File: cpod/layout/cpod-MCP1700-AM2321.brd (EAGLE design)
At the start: 11 parts

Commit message: 换用独石电容
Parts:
- moved R1 5.08 mm to (38.1, -29.2)
- moved AM2321 5.08 mm to (39.4, -31.8)
- moved MCP1700T 5.08 mm to (34.3, -34.3)
- moved C1 2.54 mm to (33.0, -36.8)
- moved C2 2.54 mm to (38.1, -36.8)
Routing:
- net GND: track 89.5 -> 84.4 mm
- net VCC: track 58.9 -> 53.8 mm
- net SDA: track 15.2 -> 20.3 mm
- net RAW: track 14.8 -> 10.8 mm
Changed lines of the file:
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@@
 </autorouter>
 <elements>
-<element name="AM2321" library="SparkFun-Connectors" package="1X04" value="" x="39.37" y="-26.67" rot="R180"/>
-<element name="MCP1700T" library="SparkFun-Connectors" package="1X03" value="+3V3" x="34.29" y="-29.21"/>
+<element name="AM2321" library="SparkFun-Connectors" package="1X04" value="" x="39.37" y="-31.75" rot="R180"/>
+<element name="MCP1700T" library="SparkFun-Connectors" package="1X03" value="+3V3" x="34.29" y="-34.29"/>
 <element name="ARDUINO1" library="SparkFun-Connectors" package="1X12" value="M12PTH" x="31.75" y="-16.51"/>
 <element name="ARDUINO2" library="SparkFun-Connectors" package="1X12" value="M12PTH" x="31.75" y="-1.27"/>
@@
 <element name="SUPPLY" library="SparkFun-Connectors" package="2X4" value="M04X2" x="40.64" y="-40.64" rot="R180"/>
 <element name="U$2" library="SparkFun-Aesthetics" package="OSHW-LOGO-L" value="" x="5.08" y="-38.1"/>
-<element name="R1" library="rcl" package="0204V" value="5.1k" x="38.1" y="-24.13"/>
-<element name="C1" library="rcl" package="C025-024X044" value="1uF" x="33.02" y="-34.29"/>
-<element name="C2" library="rcl" package="C025-024X044" value="1uF" x="38.1" y="-34.29" rot="R180"/>
+<element name="R1" library="rcl" package="0204V" value="5.1k" x="38.1" y="-29.21"/>
+<element name="C1" library="rcl" package="C025-024X044" value="1uF" x="33.02" y="-36.83"/>
+<element name="C2" library="rcl" package="C025-024X044" value="1uF" x="38.1" y="-36.83" rot="R180"/>
 </elements>
 <signals>
@@
 <contactref element="SUPPLY" pad="6"/>
 <contactref element="NRF24L01+" pad="1"/>
-<wire x1="34.29" y1="-29.21" x2="34.29" y2="-26.67" width="0.254" layer="1"/>
+<wire x1="34.29" y1="-34.29" x2="34.29" y2="-31.75" width="0.254" layer="1"/>
 <wire x1="36.83" y1="-41.91" x2="34.29" y2="-41.91" width="0.254" layer="1"/>
 <wire x1="36.83" y1="-41.91" x2="39.37" y2="-41.91" width="0.254" layer="1"/>
@@
 <wire x1="58.42" y1="-25.4" x2="58.42" y2="-41.91" width="0.254" layer="1"/>
 <contactref element="AM2321" pad="4"/>
-<wire x1="34.29" y1="-26.67" x2="31.75" y2="-26.67" width="0.254" layer="1"/>
+<wire x1="34.29" y1="-31.75" x2="31.75" y2="-31.75" width="0.254" layer="1"/>
 <contactref element="C1" pad="2"/>
 <contactref element="C2" pad="2"/>
-<wire x1="34.29" y1="-29.21" x2="34.29" y2="-34.29" width="0.254" layer="1"/>
-<wire x1="34.29" y1="-34.29" x2="36.83" y2="-34.29" width="0.254" layer="1"/>
-<wire x1="34.29" y1="-41.91" x2="34.29" y2="-34.29" width="0.254" layer="1"/>
+<wire x1="34.29" y1="-34.29" x2="34.29" y2="-36.83" width="0.254" layer="1"/>
+<wire x1="34.29" y1="-36.83" x2="36.83" y2="-36.83" width="0.254" layer="1"/>
+<wire x1="34.29" y1="-41.91" x2="34.29" y2="-36.83" width="0.254" layer="1"/>
 </signal>
 <signal name="SDA">
 <contactref element="AM2321" pad="2"/>
 <contactref element="R1" pad="1"/>
-<wire x1="36.83" y1="-26.67" x2="36.83" y2="-24.13" width="0.254" layer="1"/>
+<wire x1="36.83" y1="-31.75" x2="36.83" y2="-29.21" width="0.254" layer="1"/>
 <contactref element="ARDUINO1" pad="1"/>
-<wire x1="31.75" y1="-16.51" x2="31.75" y2="-24.13" width="0.254" layer="1"/>
-<wire x1="31.75" y1="-24.13" x2="36.83" y2="-24.13" width="0.254" layer="1"/>
+<wire x1="31.75" y1="-16.51" x2="31.75" y2="-29.21" width="0.254" layer="1"/>
+<wire x1="31.75" y1="-29.21" x2="36.83" y2="-29.21" width="0.254" layer="1"/>
 </signal>
 <signal name="VCC">
@@
 <wire x1="59.69" y1="-29.21" x2="58.42" y2="-29.21" width="0.254" layer="16"/>
 <contactref element="R1" pad="2"/>
-<wire x1="39.37" y1="-26.67" x2="39.37" y2="-24.13" width="0.254" layer="1"/>
+<wire x1="39.37" y1="-31.75" x2="39.37" y2="-29.21" width="0.254" layer="1"/>
 <wire x1="46.99" y1="-36.83" x2="44.45" y2="-39.37" width="0.254" layer="16"/>
 <wire x1="52.07" y1="-36.83" x2="46.99" y2="-36.83" width="0.254" layer="16"/>
 <contactref element="C2" pad="1"/>
-<wire x1="39.37" y1="-39.37" x2="39.37" y2="-34.29" width="0.254" layer="1"/>
+<wire x1="39.37" y1="-39.37" x2="39.37" y2="-36.83" width="0.254" layer="1"/>
 <contactref element="MCP1700T" pad="3"/>
-<wire x1="39.37" y1="-26.67" x2="39.37" y2="-29.21" width="0.254" layer="1"/>
-<wire x1="39.37" y1="-34.29" x2="39.37" y2="-29.21" width="0.254" layer="1"/>
+<wire x1="39.37" y1="-31.75" x2="39.37" y2="-34.29" width="0.254" layer="1"/>
+<wire x1="39.37" y1="-36.83" x2="39.37" y2="-34.29" width="0.254" layer="1"/>
 </signal>
 <signal name="RAW">
 <contactref element="MCP1700T" pad="2"/>
 <contactref element="RAW" pad="1"/>
-<wire x1="31.75" y1="-34.29" x2="36.83" y2="-29.21" width="0.254" layer="16"/>
+<wire x1="31.75" y1="-36.83" x2="36.83" y2="-34.29" width="0.254" layer="16"/>
 <contactref element="C1" pad="1"/>
-<wire x1="31.75" y1="-41.91" x2="31.75" y2="-34.29" width="0.254" layer="1"/>
+<wire x1="31.75" y1="-41.91" x2="31.75" y2="-36.83" width="0.254" layer="1"/>
 </signal>
 <signal name="AD3">

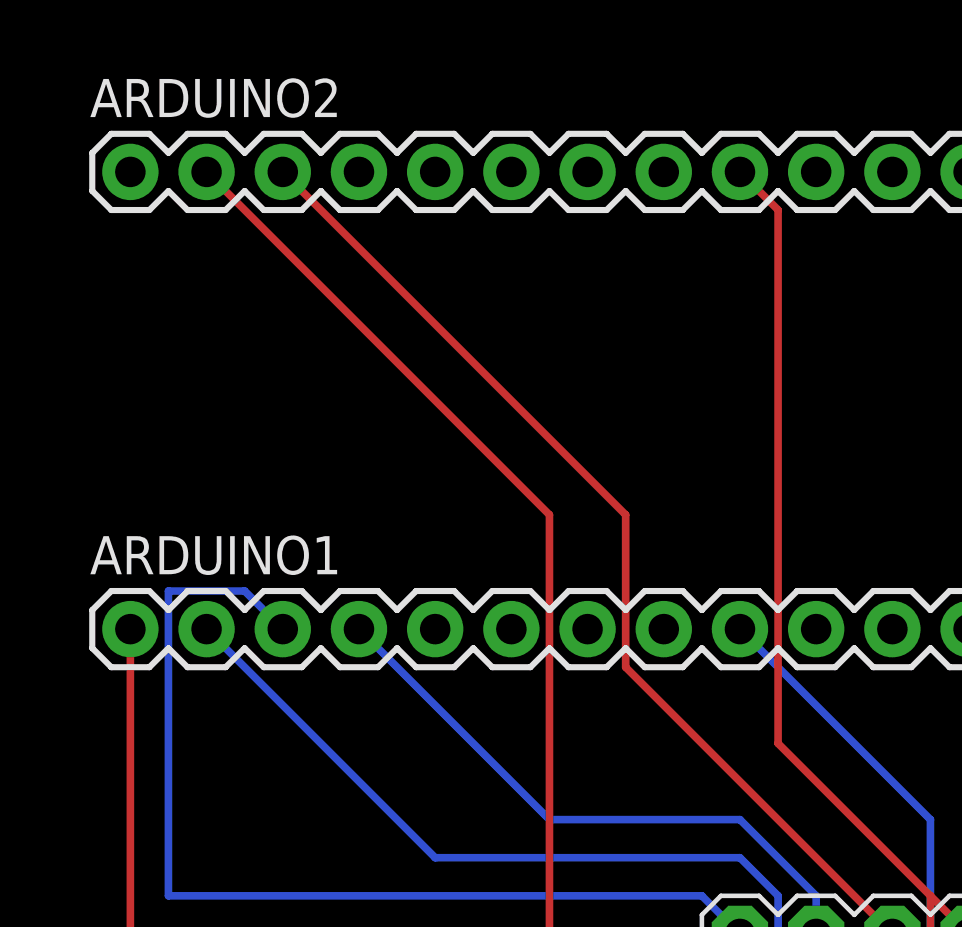
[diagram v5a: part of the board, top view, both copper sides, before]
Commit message: 增加了DS1302
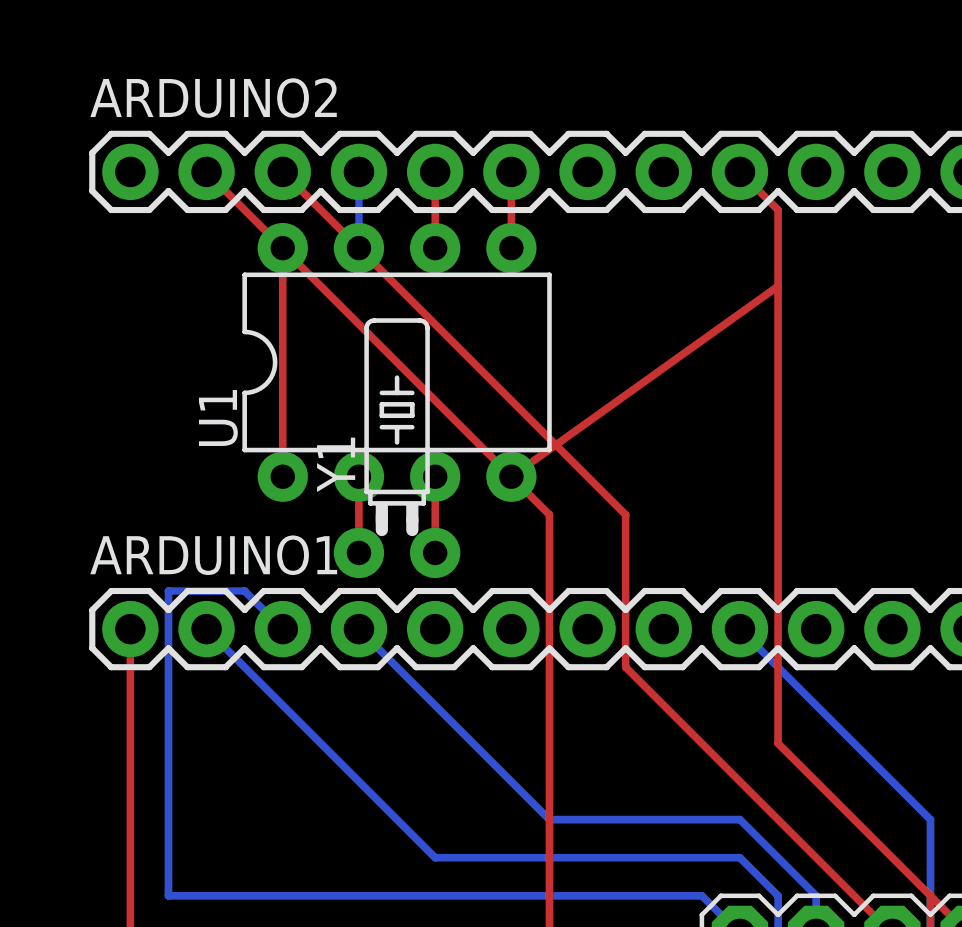
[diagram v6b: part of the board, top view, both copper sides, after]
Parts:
- added U1: DS1302, adafruit-maxim:DIL08-ROUND
- added Y1: (no value), SparkFun-FreqCtrl:TC26H
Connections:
- new net N$1: U1.2, Y1.1
- new net N$2: U1.3, Y1.2
- new net N$3: U1.1, U1.8
- net D4: now also U1.5
- net D5: now also U1.6
- net D6: now also U1.7
- net GND: now also U1.4
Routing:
- net GND: track 84.4 -> 95.4 mm
- net N$3: track 0.00 -> 7.62 mm
- net N$2: track 0.00 -> 2.54 mm
- net N$1: track 0.00 -> 2.54 mm
- net D6: track 0.00 -> 2.54 mm
- net D5: track 0.00 -> 2.54 mm
- net D4: track 0.00 -> 2.54 mm
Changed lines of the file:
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@@
 <layer number="106" name="bPlate" color="7" fill="1" visible="no" active="yes"/>
 <layer number="107" name="Crop" color="7" fill="1" visible="no" active="yes"/>
+<layer number="108" name="fp8" color="7" fill="1" visible="no" active="yes"/>
+<layer number="109" name="fp9" color="7" fill="1" visible="no" active="yes"/>
+<layer number="110" name="fp0" color="7" fill="1" visible="no" active="yes"/>
+<layer number="111" name="LPC17xx" color="7" fill="1" visible="yes" active="yes"/>
+<layer number="112" name="tSilk" color="7" fill="1" visible="yes" active="yes"/>
 <layer number="116" name="Patch_BOT" color="9" fill="4" visible="no" active="yes"/>
 <layer number="121" name="_tsilk" color="7" fill="1" visible="no" active="yes"/>
 <layer number="122" name="_bsilk" color="7" fill="1" visible="no" active="yes"/>
+<layer number="123" name="tTestmark" color="7" fill="1" visible="no" active="yes"/>
+<layer number="124" name="bTestmark" color="7" fill="1" visible="no" active="yes"/>
 <layer number="125" name="_tNames" color="7" fill="1" visible="no" active="yes"/>
+<layer number="126" name="_bNames" color="7" fill="1" visible="yes" active="yes"/>
+<layer number="127" name="_tValues" color="7" fill="1" visible="yes" active="yes"/>
+<layer number="128" name="_bValues" color="7" fill="1" visible="yes" active="yes"/>
+<layer number="131" name="tAdjust" color="7" fill="1" visible="no" active="yes"/>
+<layer number="132" name="bAdjust" color="7" fill="1" visible="no" active="yes"/>
 <layer number="144" name="Drill_legend" color="7" fill="1" visible="no" active="yes"/>
 <layer number="151" name="HeatSink" color="7" fill="1" visible="no" active="yes"/>
+<layer number="152" name="_bDocu" color="7" fill="1" visible="yes" active="yes"/>
 <layer number="199" name="Contour" color="7" fill="1" visible="yes" active="yes"/>
 <layer number="200" name="200bmp" color="1" fill="10" visible="no" active="yes"/>
@@
 <layer number="223" name="223bmp" color="24" fill="1" visible="no" active="no"/>
 <layer number="224" name="224bmp" color="25" fill="1" visible="no" active="no"/>
+<layer number="248" name="Housing" color="7" fill="1" visible="yes" active="yes"/>
+<layer number="249" name="Edge" color="7" fill="1" visible="yes" active="yes"/>
 <layer number="250" name="Descript" color="3" fill="1" visible="no" active="no"/>
 <layer number="251" name="SMDround" color="12" fill="11" visible="no" active="no"/>
@@
 <element name="C1" library="rcl" package="C025-024X044" value="1uF" x="33.02" y="-36.83"/>
 <element name="C2" library="rcl" package="C025-024X044" value="1uF" x="38.1" y="-36.83" rot="R180"/>
+<element name="U1" library="adafruit-maxim" package="DIL08-ROUND" value="DS1302" x="40.64" y="-7.62"/>
+<element name="Y1" library="SparkFun-FreqCtrl" package="TC26H" value="" x="40.64" y="-13.97"/>
 </elements>
 <signals>
@@
 <wire x1="53.34" y1="-20.32" x2="58.42" y2="-25.4" width="0.254" layer="1"/>
 <wire x1="58.42" y1="-25.4" x2="59.69" y2="-26.67" width="0.254" layer="1"/>
-<wire x1="53.34" y1="-2.54" x2="53.34" y2="-20.32" width="0.254" layer="1"/>
+<wire x1="53.34" y1="-2.54" x2="53.34" y2="-5.08" width="0.254" layer="1"/>
+<wire x1="53.34" y1="-5.08" x2="53.34" y2="-20.32" width="0.254" layer="1"/>
 <wire x1="52.07" y1="-1.27" x2="53.34" y2="-2.54" width="0.254" layer="1"/>
 <wire x1="58.42" y1="-41.91" x2="44.45" y2="-41.91" width="0.254" layer="1"/>
@@
 <wire x1="34.29" y1="-36.83" x2="36.83" y2="-36.83" width="0.254" layer="1"/>
 <wire x1="34.29" y1="-41.91" x2="34.29" y2="-36.83" width="0.254" layer="1"/>
+<contactref element="U1" pad="4"/>
+<wire x1="53.34" y1="-5.08" x2="44.45" y2="-11.43" width="0.254" layer="1"/>
 </signal>
 <signal name="SDA">
@@
 <signal name="D4">
 <contactref element="ARDUINO2" pad="6"/>
+<contactref element="U1" pad="5"/>
+<wire x1="44.45" y1="-1.27" x2="44.45" y2="-3.81" width="0.254" layer="1"/>
 </signal>
 <signal name="D5">
 <contactref element="ARDUINO2" pad="5"/>
+<contactref element="U1" pad="6"/>
+<wire x1="41.91" y1="-1.27" x2="41.91" y2="-3.81" width="0.254" layer="1"/>
 </signal>
 <signal name="D6">
 <contactref element="ARDUINO2" pad="4"/>
+<contactref element="U1" pad="7"/>
+<wire x1="39.37" y1="-1.27" x2="39.37" y2="-3.81" width="0.254" layer="16"/>
 </signal>
 <signal name="CSN">
@@
 <contactref element="NRF24L01+" pad="8"/>
 </signal>
+<signal name="N$1">
+<contactref element="U1" pad="2"/>
+<contactref element="Y1" pad="1"/>
+<wire x1="39.37" y1="-11.43" x2="39.37" y2="-13.97" width="0.254" layer="1"/>
+</signal>
+<signal name="N$2">
+<contactref element="Y1" pad="2"/>
+<contactref element="U1" pad="3"/>
+<wire x1="41.91" y1="-11.43" x2="41.91" y2="-13.97" width="0.254" layer="1"/>
+</signal>
+<signal name="N$3">
+<contactref element="U1" pad="1"/>
+<contactref element="U1" pad="8"/>
+<wire x1="36.83" y1="-3.81" x2="36.83" y2="-11.43" width="0.254" layer="1"/>
+</signal>
 </signals>
